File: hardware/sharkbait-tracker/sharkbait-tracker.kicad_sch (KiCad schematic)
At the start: 8 parts, among them U1 LLCC68, U2 STM32L031G6Ux, Y1 32MHz

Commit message: Most of the layout done, but might break things
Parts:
- removed L1: 68u, Inductor_SMD:L_0603_1608Metric, symbol Device:L
- removed U1: LLCC68, Package_DFN_QFN:QFN-24-1EP_4x4mm_P0.5mm_EP2.7x2.7mm, symbol RF_Custom:LLCC68
- removed Y1: 32MHz, Crystal:Crystal_SMD_2016-4Pin_2.0x1.6mm, symbol Device:Crystal_GND24
- added BT1: LiPo, Connector_PinHeader_2.00mm:PinHeader_1x02_P2.00mm_Vertical, symbol Device:Battery_Cell
- added C17, C18, C7, C8: 0.1uF, Capacitor_SMD:C_0402_1005Metric, symbol Device:C
- added C4: 10uF, Capacitor_SMD:C_0603_1608Metric, symbol Device:C
- added H1, H2: MountingHole, MountingHole:MountingHole_2.2mm_M2, symbol Mechanical:MountingHole
- added J1: Conn_01x04, Connector_Molex:Molex_PicoBlade_53047-0410_1x04_P1.25mm_Vertical, symbol Connector_Generic:Conn_01x04
- added JP1: RST, Jumper:SolderJumper-2_P1.3mm_Open_RoundedPad1.0x1.5mm, symbol Jumper:SolderJumper_2_Open
- added JP2: BOOT, Jumper:SolderJumper-2_P1.3mm_Open_RoundedPad1.0x1.5mm, symbol Jumper:SolderJumper_2_Open
- added JP3: Ublox_VCCIO, Jumper:SolderJumper-2_P1.3mm_Open_TrianglePad1.0x1.5mm, symbol Jumper:SolderJumper_2_Open
- added R1, R12, R2, R7, R8: 4.7k, Resistor_SMD:R_0402_1005Metric, symbol Device:R_US
- added R10, R11, R3, R4: 220, Resistor_SMD:R_0402_1005Metric, symbol Device:R_US
- added TP1: DBG_RX, TestPoint:TestPoint_Pad_D1.0mm, symbol Connector:TestPoint
- added TP2: DBG_TX, TestPoint:TestPoint_Pad_D1.0mm, symbol Connector:TestPoint
- added U1: Quectel_L96, RF_Module_Custom:CAM-M8_QuectelL96, symbol RF_Custom:Quectel_L96
- added U2: XC6206PxxxMR, Package_TO_SOT_SMD:SOT-23-3, symbol Regulator_Linear:XC6206PxxxMR
- added U3: XT25F32FDTIGT, Package_SON:Winbond_USON-8-1EP_3x2mm_P0.5mm_EP0.2x1.6mm, symbol Memory_Flash:M25PX32-VMP
- C1: value 68p -> 0.1uF; JLCPCB_CORRECTION (none) -> 0;0;90; LCSC C14441 -> C1525
- C2: value 0.1uF -> 10uF; footprint Capacitor_SMD:C_0402_1005Metric -> Capacitor_SMD:C_0603_1608Metric; JLCPCB_CORRECTION 0;0;90 -> (none); LCSC C1525 -> C19702
- renumbered R1 to R9, U2 to U5
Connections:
- net VR_PA is gone; now on net +3.3V: C1.1, C2.1
- net +3.3V: now also C17.1, C18.1, C7.1, C8.1, JP2.2 (B), JP3.1 (A), R1.1, R12.1, R2.1, R8.1, U1.8 (V_BCKP), U1.9 (VCC), U2.2 (VO), U3.3 (~{W}/V_{PP}), U3.7 (~{HOLD}), U3.8 (V_{CC}); no longer R9.2
- net GND: now also D1.1 (K), BT1.2 (-), C17.2, C18.2, C4.2, C7.2, C8.2, J1.4 (Pin_4), JP1.1 (A), R7.2, U1.10 (GND), U1.11 (GND), U1.12 (GND), U1.13 (GND), U1.14 (GND), U1.15 (GND), U1.18 (GND), U1.19 (GND), U1.21 (GND), U1.22 (GND), U1.27 (GND), U1.31 (GND), U1.4 (GND), U1.5 (GND), U2.1 (GND), U3.4 (V_{SS}), U3.9 (PAD/V_{SS})
- net LED: now also R9.2, U5.3 (PC15); no longer D1.1 (K)
- net MISO: now also U3.2 (DQ1)
- net MOSI: now also U3.5 (DQ0)
- net SCK: now also U3.6 (C)
- net RF_CS: now reaches U5.10 (PA4)
- net GPS_nRST: now reaches U5.18 (PA8)
- net GPS_nRST: now also R11.2
- net DBG_TX: now reaches U5.19 (PA9)
- net DBG_TX: now also TP2.1
- net DBG_RX: now reaches U5.20 (PA10)
- net DBG_RX: now also TP1.1
- net SWDIO: now reaches U5.21 (PA13)
- net SWDIO: now also J1.2 (Pin_2)
- net SWCLK: now reaches U5.22 (PA14)
- net SWCLK: now also J1.3 (Pin_3)
- net FLASH_CS: now reaches U5.23 (PA15)
- net FLASH_CS: now also U3.1 (~{S})
- net BOOT: now reaches U5.27 (BOOT0)
- net BOOT: now also JP2.1 (A), R7.1
- net NRST: now reaches U5.4 (NRST)
- net NRST: now also JP1.2 (B), R8.2
- net GPS_1PPS: now reaches U5.6 (PA0)
- net GPS_1PPS: now also R10.2
- net TX: now reaches U5.8 (PA2)
- net TX: now also R4.2
- net RX: now reaches U5.9 (PA3)
- net RX: now also R3.2
- net MISO_alt renamed RF_nRST
- net MOSI_alt renamed RF_BUSY
- net SCK_alt renamed OWI
- net OWI: now also J1.1 (Pin_1), R12.2
- new net: U1.16 (RF_OUT), U1.17 (RF_IN)
- new net +BATT: BT1.1 (+), C4.1, U2.3 (VI)
- new net GPS_RX: R4.1, U1.26 (RXD)
- new net GPS_TX: R3.1, U1.25 (TXD)
- new net R_1PPS: R10.1, U1.29 (TIMEPULSE)
- new net R_nRST: R11.1, U1.23 (RESET_N)
- new net SCL_NC: R1.2, U1.6 (SCL)
- new net SDA_NC: R2.2, U1.3 (SDA)
- new net UBLOX_VCCIO: JP3.2 (B), U1.1 (NC)
- no-connect marks 0 -> 9
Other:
- added sheet RF Transmitter (rf_tx.kicad_sch)
- note removed: "PA bias stage Inductor is self resonant at 900MHz which is a good thing I guess? Capacitors picked based on STM application note except I cranked the bulk decoupling for availability"
- moved on the sheet: D1, R9, U5

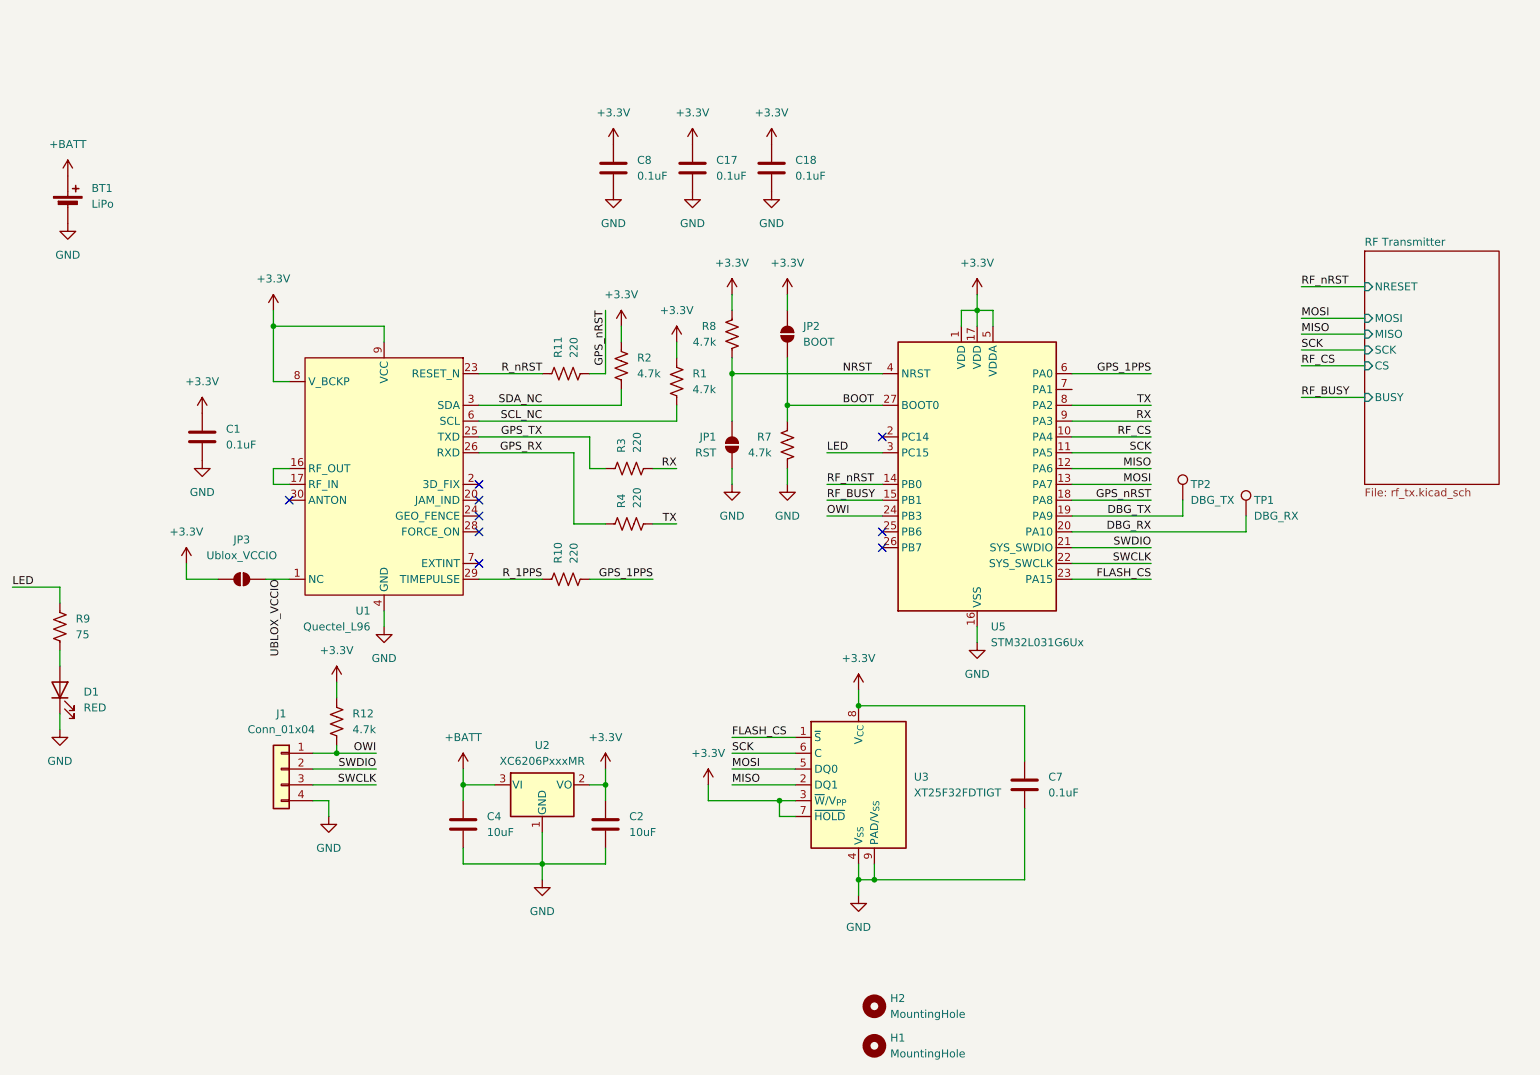
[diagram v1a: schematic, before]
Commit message: Everything fits, might rearrange a little
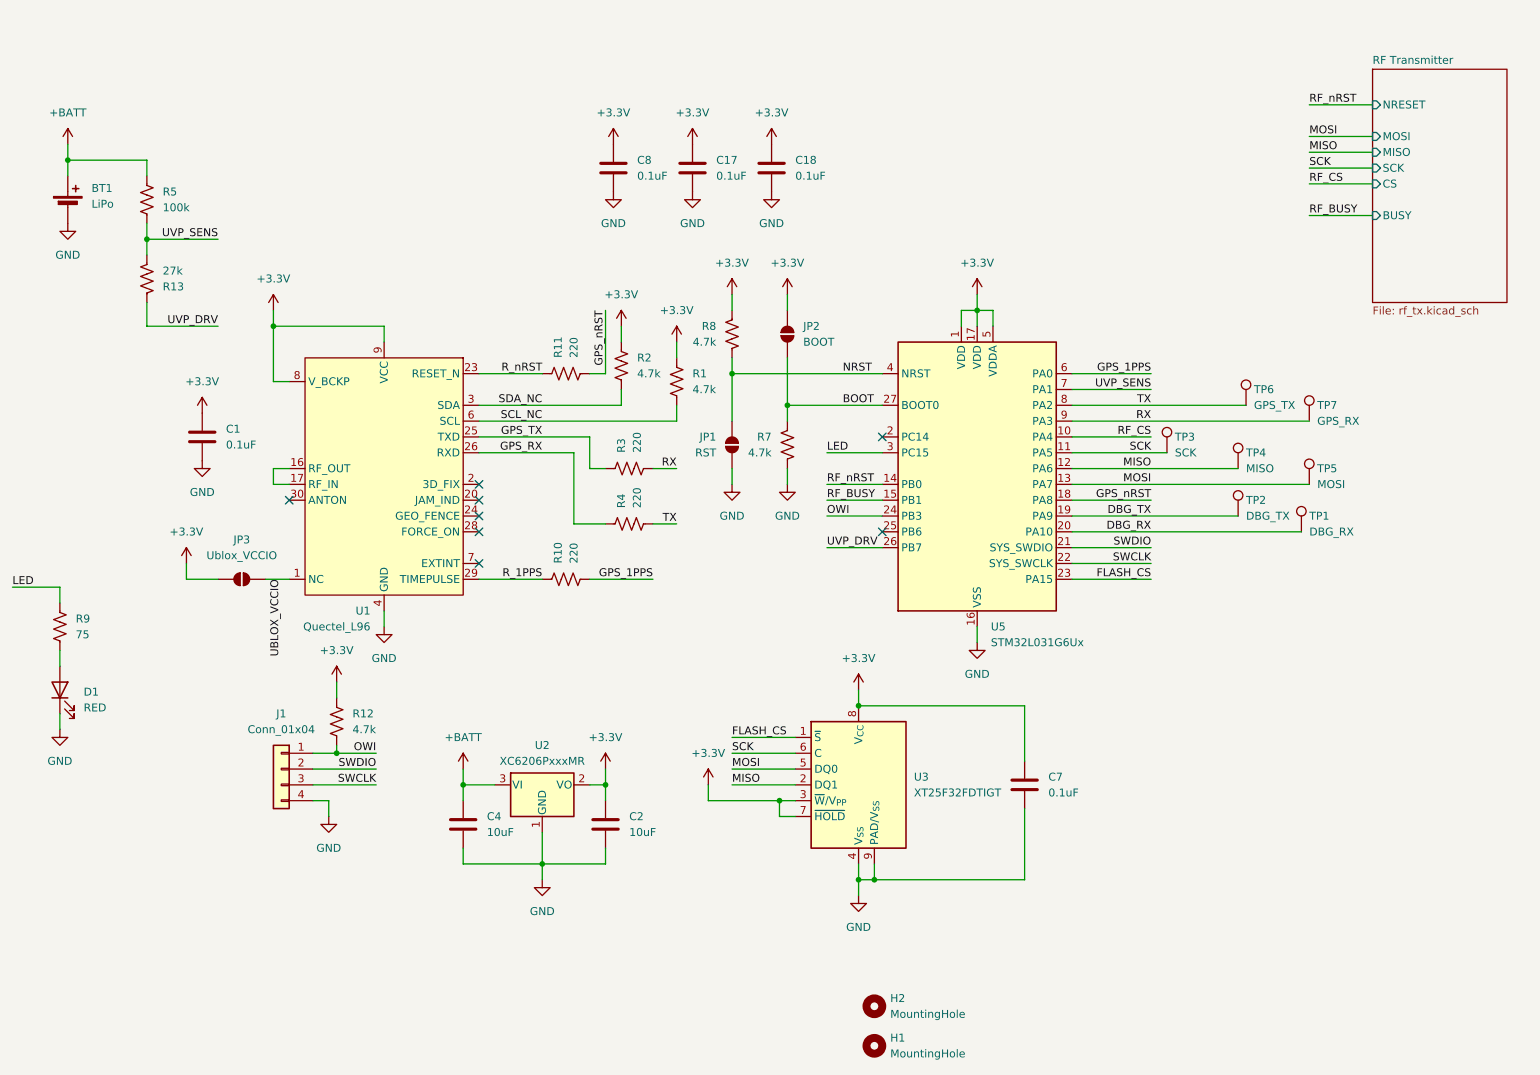
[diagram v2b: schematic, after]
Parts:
- added R13: 27k, Resistor_SMD:R_0402_1005Metric, symbol Device:R_US
- added R5: 100k, Resistor_SMD:R_0402_1005Metric, symbol Device:R_US
- added TP3: SCK, TestPoint:TestPoint_Pad_D1.0mm, symbol Connector:TestPoint
- added TP4: MISO, TestPoint:TestPoint_Pad_D1.0mm, symbol Connector:TestPoint
- added TP5: MOSI, TestPoint:TestPoint_Pad_D1.0mm, symbol Connector:TestPoint
- added TP6: GPS_TX, TestPoint:TestPoint_Pad_D1.0mm, symbol Connector:TestPoint
- added TP7: GPS_RX, TestPoint:TestPoint_Pad_D1.0mm, symbol Connector:TestPoint
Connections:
- net +BATT: now also R5.1
- net MISO: now also TP4.1
- net MOSI: now also TP5.1
- net RX: now also TP7.1
- net SCK: now also TP3.1
- net TX: now also TP6.1
- net UVP_DRV: now reaches U5.26 (PB7)
- net UVP_DRV: now also R13.1
- net UVP_SENS: now reaches U5.7 (PA1)
- net UVP_SENS: now also R13.2, R5.2
- no-connect marks 9 -> 8
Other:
- moved on the sheet: TP1, TP2

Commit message: Removed battery voltage divider again, and rounded corners
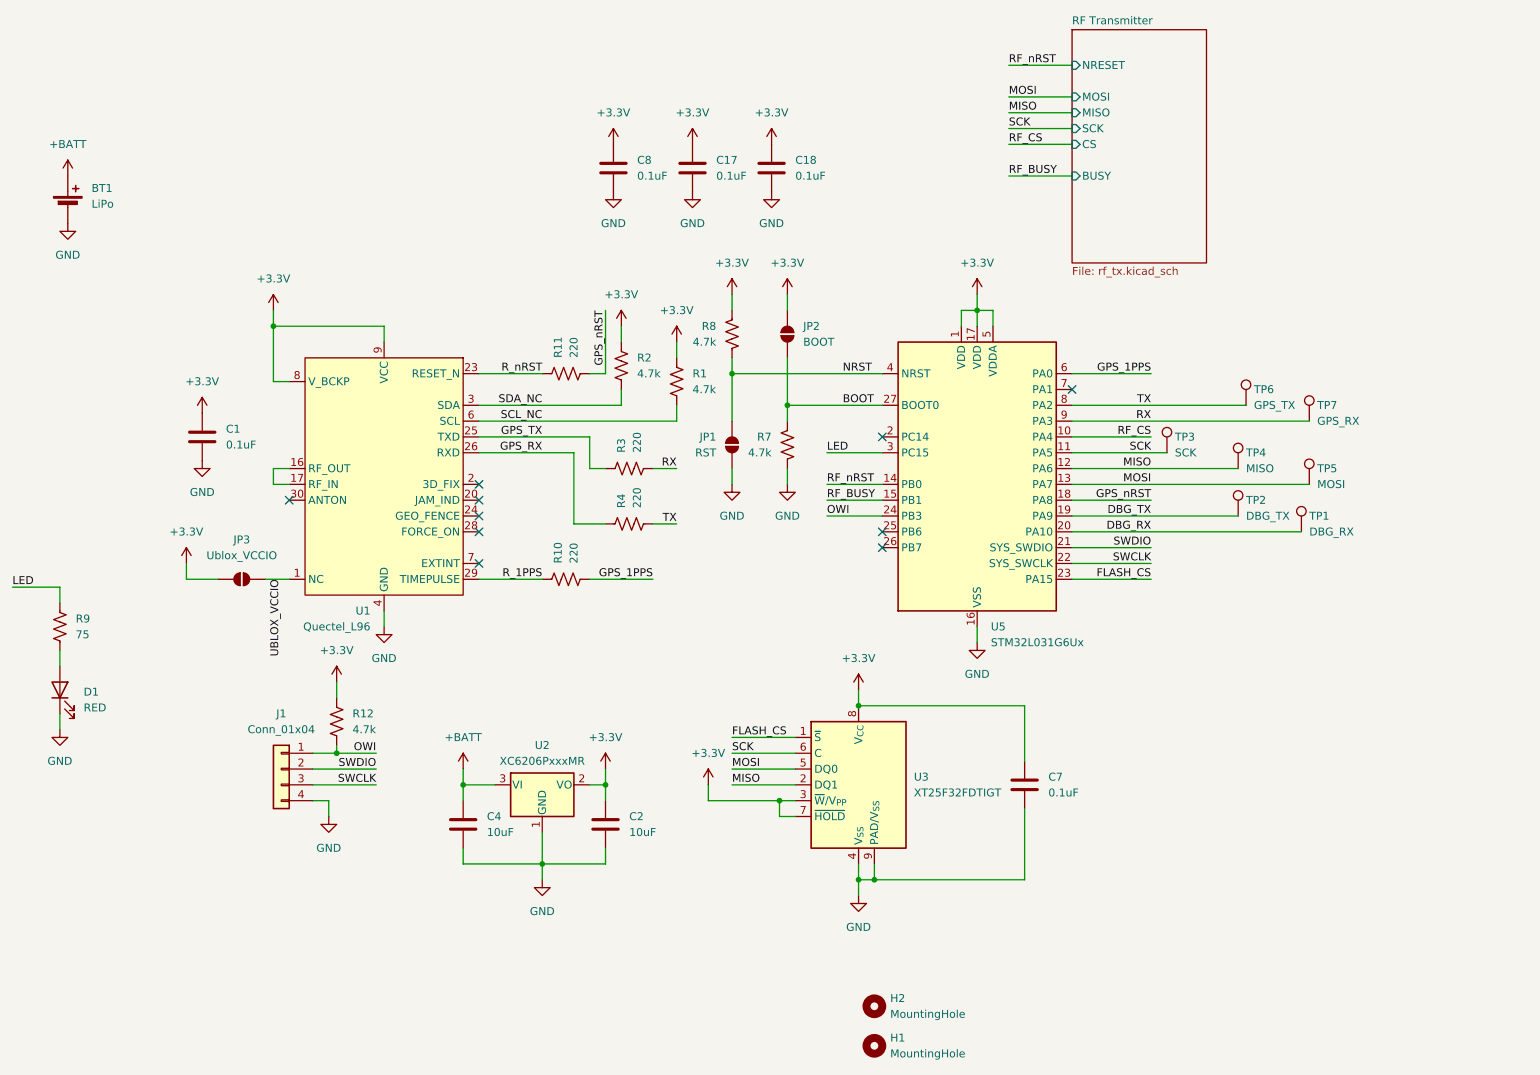
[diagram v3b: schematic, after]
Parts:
- removed R13: 27k, Resistor_SMD:R_0402_1005Metric, symbol Device:R_US
- removed R5: 100k, Resistor_SMD:R_0402_1005Metric, symbol Device:R_US
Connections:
- net UVP_DRV: no longer names the net of U5.26 (PB7)
- net UVP_SENS: no longer names the net of U5.7 (PA1)
- no-connect marks 8 -> 10

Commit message: Combination antenna footprint and build automation
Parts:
- C1, C17, C18, C7, C8: JLCPCB_CORRECTION 0;0;90 -> (none)
- R1, R12, R2, R7, R8: LCSC C2906941 -> C25900
- R10, R11, R3, R4: LCSC (none) -> C25091
- U1: JLCPCB_CORRECTION (none) -> 0;7.52;180; LCSC (none) -> C5197298
- U2: JLCPCB_CORRECTION (none) -> 0;0;180
- U3: JLCPCB_CORRECTION (none) -> 0;0;-90; LCSC (none) -> C7429719
- U5: JLCPCB_CORRECTION (none) -> 0;0;-90; LCSC (none) -> C96514
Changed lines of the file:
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@@
 			)
 		)
-		(property "JLCPCB_CORRECTION" "0;0;90"
+		(property "JLCPCB_CORRECTION" ""
 			(at 129.54 54.61 0)
 			(effects
@@
 			)
 		)
-		(property "LCSC" "C2906941"
+		(property "LCSC" "C25900"
 			(at 144.78 99.06 0)
 			(effects
@@
 			)
 		)
-		(property "JLCPCB_CORRECTION" "0;0;90"
+		(property "JLCPCB_CORRECTION" ""
 			(at 116.84 54.61 0)
 			(effects
@@
 			)
 		)
-		(property "LCSC" "C2906941"
+		(property "LCSC" "C25900"
 			(at 135.89 81.28 0)
 			(effects
@@
 			)
 		)
-		(property "JLCPCB_CORRECTION" "0;0;90"
+		(property "JLCPCB_CORRECTION" ""
 			(at 182.88 153.67 0)
 			(effects
@@
 			)
 		)
+		(property "LCSC" "C96514"
+			(at 175.26 105.41 0)
+			(effects
+				(font
+					(size 1.27 1.27)
+				)
+				(hide yes)
+			)
+		)
+		(property "JLCPCB_CORRECTION" "0;0;-90"
+			(at 175.26 105.41 0)
+			(effects
+				(font
+					(size 1.27 1.27)
+				)
+				(hide yes)
+			)
+		)
 		(pin "19"
 		)
@@
 			)
 		)
-		(property "LCSC" "C2906941"
+		(property "LCSC" "C25900"
 			(at 72.39 143.51 0)
 			(effects
@@
 			)
 		)
-		(property "JLCPCB_CORRECTION" "0;0;90"
+		(property "JLCPCB_CORRECTION" ""
 			(at 142.24 54.61 0)
 			(effects
@@
 			)
 		)
-		(property "LCSC" ""
+		(property "LCSC" "C25091"
 			(at 119.38 102.87 0)
 			(effects
@@
 			)
 		)
+		(property "LCSC" "C5197298"
+			(at 80.01 105.41 0)
+			(effects
+				(font
+					(size 1.27 1.27)
+				)
+				(hide yes)
+			)
+		)
+		(property "JLCPCB_CORRECTION" "0;7.52;180"
+			(at 80.01 105.41 0)
+			(effects
+				(font
+					(size 1.27 1.27)
+				)
+				(hide yes)
+			)
+		)
 		(pin "18"
 		)
@@
 			)
 		)
-		(property "LCSC" ""
+		(property "LCSC" "C25091"
 			(at 109.22 87.63 0)
 			(effects
@@
 			)
 		)
-		(property "LCSC" "C2906941"
+		(property "LCSC" "C25900"
 			(at 118.11 86.36 0)
 			(effects
@@
 			)
 		)
+		(property "LCSC" "C7429719"
+			(at 156.21 153.67 0)
+			(effects
+				(font
+					(size 1.27 1.27)
+				)
+				(hide yes)
+			)
+		)
+		(property "JLCPCB_CORRECTION" "0;0;-90"
+			(at 156.21 153.67 0)
+			(effects
+				(font
+					(size 1.27 1.27)
+				)
+				(hide yes)
+			)
+		)
 		(pin "1"
 		)
@@
 			)
 		)
-		(property "LCSC" ""
+		(property "LCSC" "C25091"
 			(at 119.38 111.76 0)
 			(effects
@@
 			)
 		)
-		(property "JLCPCB_CORRECTION" "0;0;90"
+		(property "JLCPCB_CORRECTION" ""
 			(at 50.8 97.79 0)
 			(effects
@@
 			)
 		)
-		(property "JLCPCB_CORRECTION" ""
+		(property "JLCPCB_CORRECTION" "0;0;180"
 			(at 105.41 153.67 0)
 			(effects
@@
 			)
 		)
-		(property "LCSC" "C2906941"
+		(property "LCSC" "C25900"
 			(at 127 88.9 0)
 			(effects
@@
 			)
 		)
-		(property "LCSC" ""
+		(property "LCSC" "C25091"
 			(at 109.22 120.65 0)
 			(effects

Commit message: Updated vias for easier tolerances
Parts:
- D1: JLCPCB_CORRECTION 0;0;180 -> (none)
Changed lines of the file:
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@@
 			)
 		)
-		(property "JLCPCB_CORRECTION" "0;0;180"
+		(property "JLCPCB_CORRECTION" ""
 			(at 27.94 138.43 0)
 			(effects
